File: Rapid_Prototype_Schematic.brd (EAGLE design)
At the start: 142 x 95 mm, 177 parts, among them IC2 SI4459ADY-T1-GE3, IC8 SI4485DY-T1-GE3, J1 XT60-M, J10 XT60-M, J2 XT60-M, J3 Vertical Qwiic Connector, J4 UJ2-MIBH-2-SMT-TR-67, J5 XT60-M, J6 XT60-M, J7 XT60-M, J8 XT60-M, J9 XT60-M, Q1 LTV-8141S, Q10 SI4435DDY, Q11 DMN65D8LFB-7, Q12 SI4435DDY, Q13 DMN65D8LFB-7, Q14 SI4435DDY, Q15 DMN65D8LFB-7, Q16 2N7002PW, Q2 2N7002PW, Q3 DMN65D8LFB-7, Q4 SI4435DDY, Q5 DMN65D8LFB-7, Q6 SI4435DDY, Q7 DMN65D8LFB-7, Q8 SI4435DDY, Q9 DMN65D8LFB-7, U1 LM35DM, U2 LM2904ITPX/NOPB, U3 LM2904ITPX/NOPB, U4 LM2904ITPX/NOPB, U5 LM2904ITPX/NOPB, U6 LM2904ITPX/NOPB, U7 TLV1117LV33DCYR, U8 LT1374IS8-5PBF

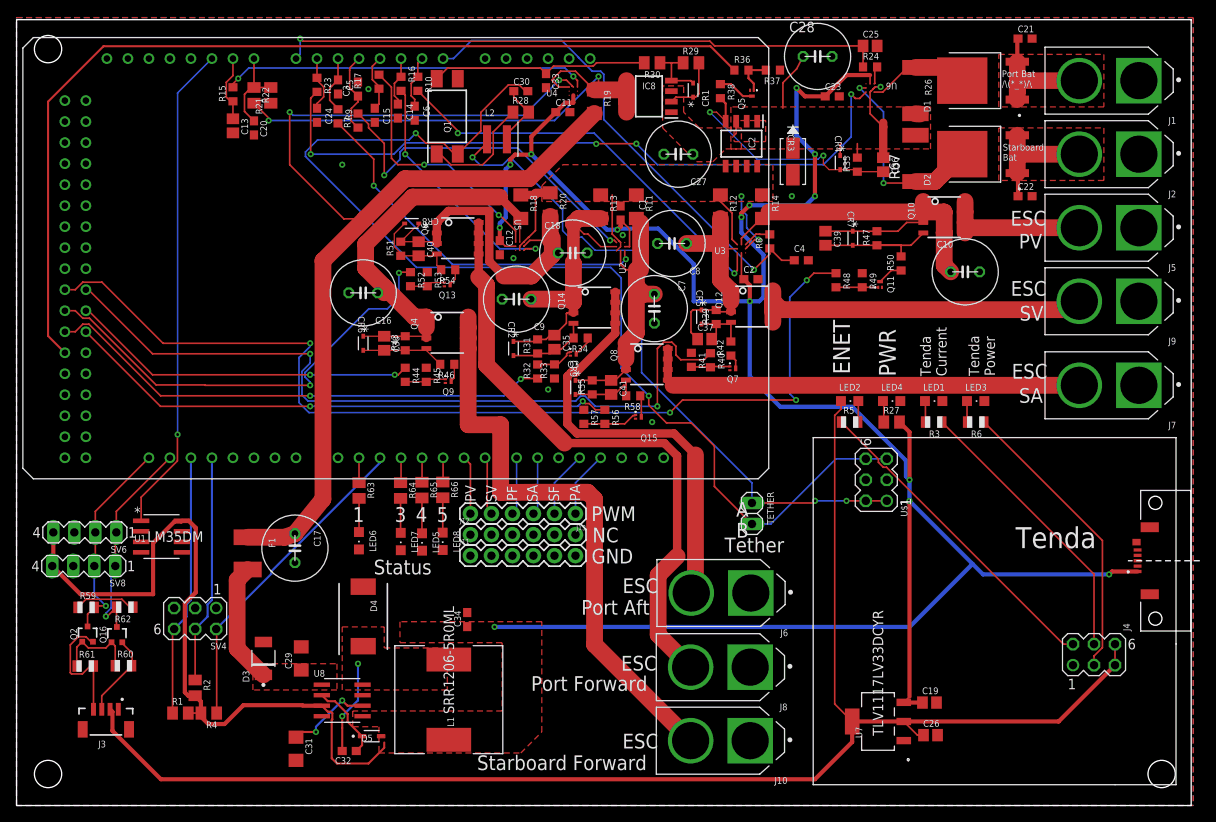
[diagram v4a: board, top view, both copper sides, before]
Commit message: Capacitor Size Changes
Replaced and made capacitors smaller
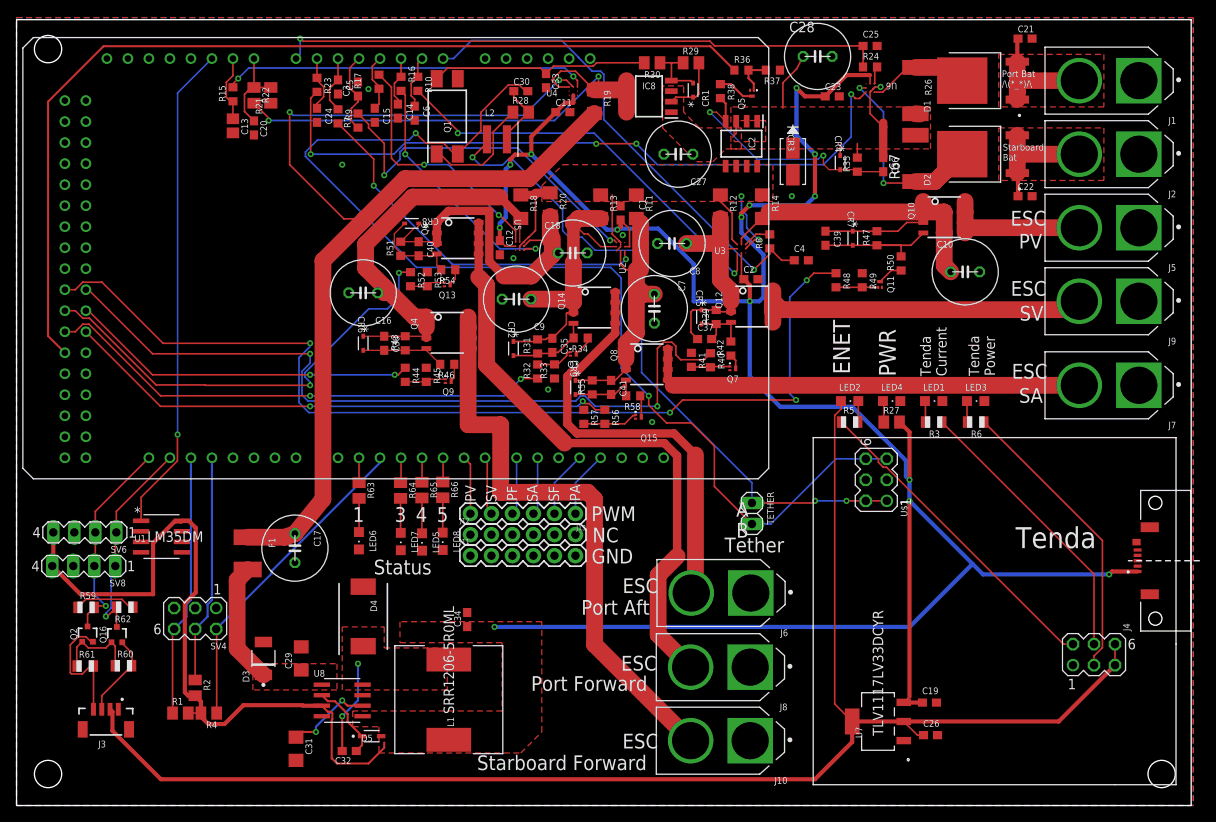
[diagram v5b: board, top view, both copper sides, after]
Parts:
- C19, C25, C26, C35, C36, C37, C38, C39, C40, C41: value 1µF -> 1.0uF; device adafruit:C0805 -> SparkFun-Capacitors:0603
- C24: value 1µF -> 1.0uF; device adafruit:C0603 -> SparkFun-Capacitors:0603
- moved C35 0.45 mm to (64.8, 55.6)

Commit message: Changing units in Schematic
Changed C11 and C30 from 100nF to 0.1 uF, this allows us to order those parts without needing quantity change
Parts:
- C11: value 100nF -> 0.1uF
- C30: value 100nf -> 0.1uF
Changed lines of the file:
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@@
 <attribute name="VALUE" x="111.506" y="62.357" size="1.27" layer="27" ratio="10"/>
 </element>
-<element name="C11" library="adafruit" library_urn="urn:adsk.eagle:library:420" package="C0603" package3d_urn="urn:adsk.eagle:package:6240338/1" value="100nF" x="66.04" y="83.82" smashed="yes">
+<element name="C11" library="adafruit" library_urn="urn:adsk.eagle:library:420" package="C0603" package3d_urn="urn:adsk.eagle:package:6240338/1" value="0.1uF" x="66.04" y="83.82" smashed="yes">
 <attribute name="NAME" x="65.151" y="84.582" size="0.8128" layer="25"/>
 <attribute name="VALUE" x="65.151" y="81.788" size="1.27" layer="27"/>
@@
 <attribute name="VALUE" x="43.561" y="85.725" size="1.27" layer="27" rot="R90"/>
 </element>
-<element name="C30" library="adafruit" library_urn="urn:adsk.eagle:library:420" package="C0603" package3d_urn="urn:adsk.eagle:package:6240338/1" value="100nf" x="60.96" y="86.36" smashed="yes">
+<element name="C30" library="adafruit" library_urn="urn:adsk.eagle:library:420" package="C0603" package3d_urn="urn:adsk.eagle:package:6240338/1" value="0.1uF" x="60.96" y="86.36" smashed="yes">
 <attribute name="NAME" x="60.071" y="87.122" size="0.8128" layer="25"/>
 <attribute name="VALUE" x="60.071" y="84.328" size="1.27" layer="27"/>
